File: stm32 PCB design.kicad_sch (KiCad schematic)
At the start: 13 parts, among them SW1 SW_SPDT, U1 STM32F103C8T6

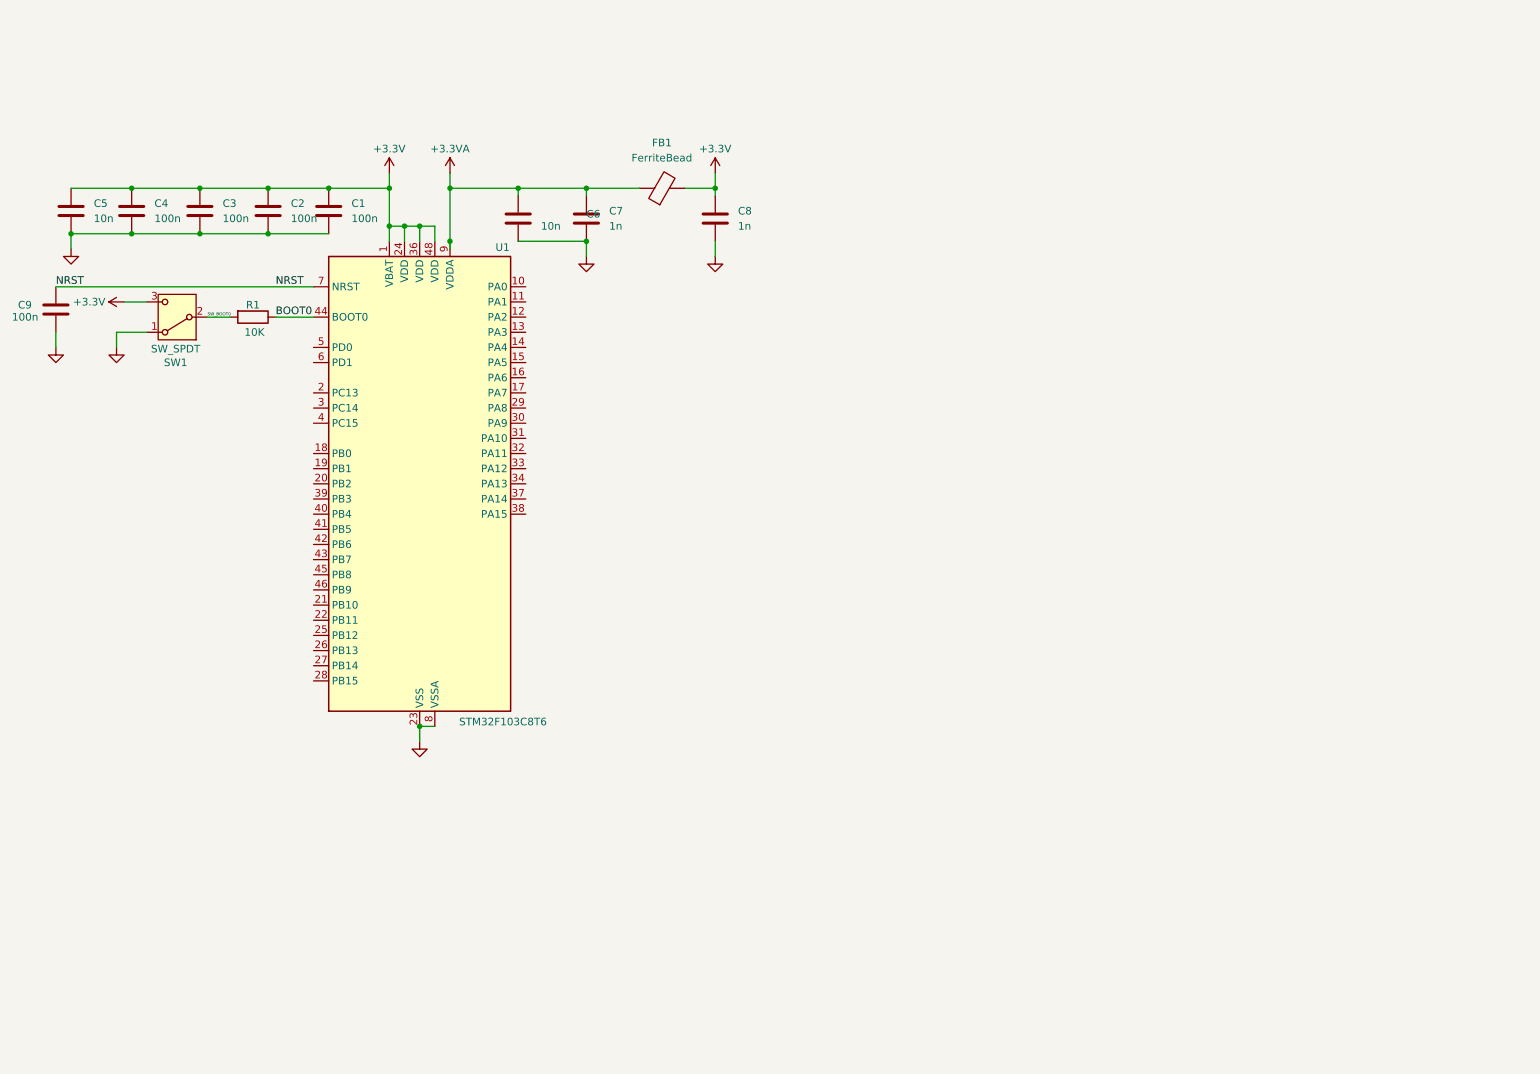
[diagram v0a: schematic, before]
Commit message: Schematic labelled and complete. EAD verified
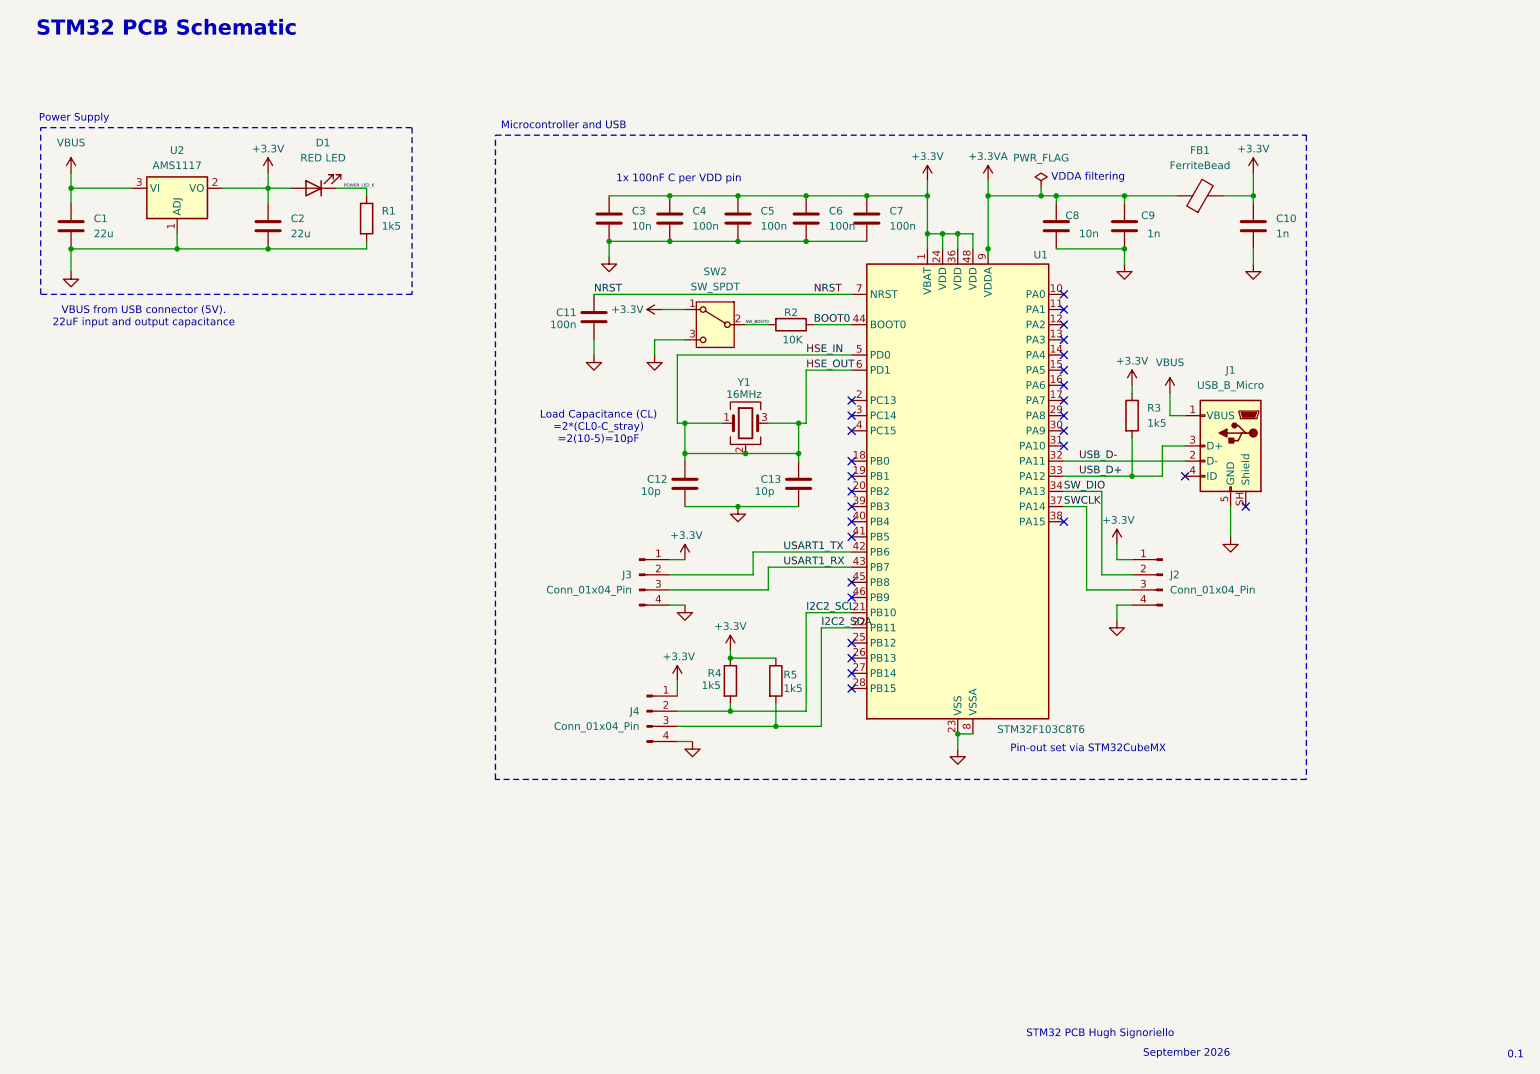
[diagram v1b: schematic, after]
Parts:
- removed SW1: SW_SPDT, symbol Switch:SW_SPDT
- added C1, C2: 22u, symbol Device:C
- added C12, C13: 10p, symbol Device:C
- added D1: RED LED, symbol Device:LED
- added J1: USB_B_Micro, symbol Connector:USB_B_Micro
- added J2, J3, J4: Conn_01x04_Pin, symbol Connector:Conn_01x04_Pin
- added R1, R3, R4, R5: 1k5, symbol Device:R
- added SW2: SW_SPDT, symbol Switch:SW_SPDT
- added U2: AMS1117, Package_TO_SOT_SMD:SOT-223-3_TabPin2, symbol Regulator_Linear:AMS1117
- added Y1: 16MHz, symbol Device:Crystal_GND24
- renumbered C8 to C10, C9 to C11, C5 to C3, C3 to C5, C2 to C6, C1 to C7, C6 to C8, C7 to C9, R1 to R2
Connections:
- net +3.3V: now also C2.1, D1.2 (A), J2.1 (Pin_1), J3.1 (Pin_1), J4.1 (Pin_1), R3.1, R4.1, R5.1, SW2.1 (A), U2.2 (VO)
- net SW_BOOT0: now also SW2.2 (B)
- net I2C2_SCL: now reaches U1.21 (PB10)
- net I2C2_SCL: now also J4.2 (Pin_2), R4.2
- net I2C2_SDA: now reaches U1.22 (PB11)
- net I2C2_SDA: now also J4.3 (Pin_3), R5.2
- net USB_D-: now reaches U1.32 (PA11)
- net USB_D-: now also J1.2 (D-)
- net USB_D+: now reaches U1.33 (PA12)
- net USB_D+: now also J1.3 (D+), R3.2
- net SW_DIO: now reaches U1.34 (PA13)
- net SW_DIO: now also J2.2 (Pin_2)
- net SWCLK: now reaches U1.37 (PA14)
- net SWCLK: now also J2.3 (Pin_3)
- net USART1_TX: now reaches U1.42 (PB6)
- net USART1_TX: now also J3.2 (Pin_2)
- net USART1_RX: now reaches U1.43 (PB7)
- net USART1_RX: now also J3.3 (Pin_3)
- net HSE_IN: now reaches U1.5 (PD0)
- net HSE_IN: now also U1.6 (PD1), C12.1, C13.1, Y1.1, Y1.2 (G), Y1.3, Y1.4 (G)
- new net: C1.2, C2.2, R1.2, U2.1 (ADJ)
- new net: C12.2, C13.2
- new net POWER_LED_K: D1.1 (K), R1.1
- new net VBUS: C1.1, J1.1 (VBUS), U2.3 (VI)
- no-connect marks 0 -> 29
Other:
- note added: "0.1"
- note added: "1x 100nF C per VDD pin"
- note added: "Load Capacitance (CL) =2*(CL0-C_stray) =2(10-5)=10pF"
- note added: "Microcontroller and USB"
- note added: "Pin-out set via STM32CubeMX"
- note added: "Power Supply"
- note added: "STM32 PCB Hugh Signoriello"
- note added: "STM32 PCB Schematic"
- note added: "September 2026"
- note added: "VBUS from USB connector (5V). 22uF input and output capacitance"
- note added: "VDDA filtering"
- moved on the sheet: C10, C11, C3, C4, C5, C6, C7, C8, C9, FB1, R2, U1

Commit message: Update PCB layout and add mounting holes
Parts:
- added H1, H2, H3, H4: MountingHole, MountingHole:MountingHole_2.2mm_M2, symbol Mechanical:MountingHole
- C1, C2: footprint (none) -> Capacitor_SMD:C_0805_2012Metric
- C10, C9: value 1n -> 1u; footprint (none) -> Capacitor_SMD:C_01005_0402Metric
- C11, C12, C13, C4, C5, C6, C7, C8: footprint (none) -> Capacitor_SMD:C_01005_0402Metric
- C3: footprint (none) -> Capacitor_SMD:C_0603_1608Metric
- D1: footprint (none) -> LED_SMD:LED_0603_1608Metric_Pad1.05x0.95mm_HandSolder
- FB1: footprint (none) -> Inductor_SMD:L_0603_1608Metric
- J1: footprint (none) -> Connector_USB:USB_Micro-B_Wuerth_629105150521
- J2, J3, J4: footprint (none) -> Connector_PinHeader_2.54mm:PinHeader_1x04_P2.54mm_Vertical
- R1, R2, R3, R4, R5: footprint (none) -> Resistor_SMD:R_0402_1005Metric
- SW2: footprint (none) -> Button_Switch_SMD:SW_SPDT_PCM12
- Y1: footprint (none) -> Crystal:Crystal_SMD_3225-4Pin_3.2x2.5mm
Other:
- note added: "Mounting Holes (M2)"

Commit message: Documentation updated and design rule checks validated
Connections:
- net HSE_IN: no longer C13.1, U1.6 (PD1), Y1.2 (G), Y1.3, Y1.4 (G)
- net GND: now reaches U1.23 (VSS), U1.35 (VSS), U1.47 (VSS), U1.8 (VSSA)
- net GND: now also C1.2, C10.2, C11.2, C12.2, C13.2, C2.2, C3.2, C4.2, C5.2, C6.2, C7.2, C8.2, C9.2, J1.5 (GND), J2.4 (Pin_4), J3.4 (Pin_4), J4.4 (Pin_4), R1.2, SW2.3 (C), U2.1 (ADJ), Y1.2 (G), Y1.4 (G)
- new net HSE_OUT: C13.1, U1.6 (PD1), Y1.3
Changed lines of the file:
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@@
 	)
 	(junction
-		(at 132.08 92.71)
-		(diameter 0)
-		(color 0 0 0 0)
-	)
-	(junction
 		(at 29.21 48.26)
 		(diameter 0)
@@
 	)
 	(junction
+		(at 142.24 101.6)
+		(diameter 0)
+		(color 0 0 0 0)
+	)
+	(junction
 		(at 46.99 58.42)
 		(diameter 0)
@@
 	)
 	(junction
-		(at 151.13 92.71)
-		(diameter 0)
-		(color 0 0 0 0)
-	)
-	(junction
-		(at 142.24 92.71)
-		(diameter 0)
-		(color 0 0 0 0)
-	)
-	(junction
 		(at 151.13 87.63)
 		(diameter 0)
@@
 	(wire
 		(pts
+			(xy 142.24 92.71) (xy 142.24 101.6)
+		)
+		(stroke
+			(width 0)
+			(type default)
+		)
+	)
+	(wire
+		(pts
 			(xy 199.39 115.57) (xy 207.01 115.57)
 		)
@@
 	(wire
 		(pts
-			(xy 142.24 92.71) (xy 151.13 92.71)
-		)
-		(stroke
-			(width 0)
-			(type default)
-		)
-	)
-	(wire
-		(pts
 			(xy 199.39 101.6) (xy 199.39 115.57)
 		)
@@
 	(wire
 		(pts
-			(xy 146.05 115.57) (xy 129.54 115.57)
+			(xy 142.24 101.6) (xy 151.13 101.6)
 		)
 		(stroke
@@
 	(wire
 		(pts
-			(xy 132.08 92.71) (xy 132.08 93.98)
+			(xy 146.05 115.57) (xy 129.54 115.57)
 		)
 		(stroke
@@
 	(wire
 		(pts
-			(xy 132.08 87.63) (xy 132.08 92.71)
+			(xy 132.08 87.63) (xy 132.08 93.98)
 		)
 		(stroke
@@
 	(wire
 		(pts
+			(xy 116.84 73.66) (xy 116.84 76.2)
+		)
+		(stroke
+			(width 0)
+			(type default)
+		)
+	)
+	(wire
+		(pts
 			(xy 147.32 138.43) (xy 154.94 138.43)
 		)
@@
 	(wire
 		(pts
-			(xy 151.13 87.63) (xy 151.13 92.71)
+			(xy 151.13 87.63) (xy 151.13 93.98)
 		)
 		(stroke
@@
 	(wire
 		(pts
-			(xy 116.84 73.66) (xy 116.84 76.2)
-		)
-		(stroke
-			(width 0)
-			(type default)
-		)
-	)
-	(wire
-		(pts
 			(xy 213.36 82.55) (xy 213.36 86.36)
 		)
@@
 	(wire
 		(pts
-			(xy 142.24 92.71) (xy 132.08 92.71)
-		)
-		(stroke
-			(width 0)
-			(type default)
-		)
-	)
-	(wire
-		(pts
 			(xy 128.27 68.58) (xy 132.08 68.58)
 		)
@@
 	(wire
 		(pts
-			(xy 151.13 92.71) (xy 151.13 93.98)
-		)
-		(stroke
-			(width 0)
-			(type default)
-		)
-	)
-	(wire
-		(pts
 			(xy 182.88 46.99) (xy 182.88 49.53)
 		)
@@
 	(wire
 		(pts
-			(xy 140.97 101.6) (xy 151.13 101.6)
+			(xy 140.97 101.6) (xy 142.24 101.6)
 		)
 		(stroke
@@
 			)
 		)
-		(property "Value" ""
+		(property "Value" "GND"
 			(at 127 81.28 0)
+			(hide yes)
 			(show_name no)
 			(do_not_autoplace no)
@@
 			)
 		)
-		(property "Value" ""
+		(property "Value" "GND"
 			(at 133.35 146.05 0)
+			(hide yes)
 			(show_name no)
 			(do_not_autoplace no)
@@
 			)
 		)
-		(property "Value" ""
+		(property "Value" "GND"
 			(at 223.52 111.76 0)
+			(hide yes)
 			(show_name no)
 			(do_not_autoplace no)
@@
 			)
 		)
-		(property "Value" ""
+		(property "Value" "GND"
 			(at 116.84 81.28 0)
+			(hide yes)
 			(show_name no)
 			(do_not_autoplace no)
@@
 			)
 		)
-		(property "Value" ""
+		(property "Value" "GND"
 			(at 29.21 67.31 0)
 			(show_name no)
@@
 			)
 		)
-		(property "Value" ""
+		(property "Value" "GND"
 			(at 204.47 125.73 0)
+			(hide yes)
 			(show_name no)
 			(do_not_autoplace no)
@@
 			)
 		)
-		(property "Value" ""
+		(property "Value" "GND"
 			(at 205.74 66.04 0)
+			(hide yes)
 			(show_name no)
 			(do_not_autoplace no)
@@
 			)
 		)
-		(property "Value" ""
+		(property "Value" "GND"
 			(at 119.38 64.77 0)
 			(show_name no)
@@
 			)
 		)
-		(property "Value" ""
+		(property "Value" "GND"
 			(at 177.8 147.32 0)
+			(hide yes)
 			(show_name no)
 			(do_not_autoplace no)
@@
 			)
 		)
-		(property "Value" ""
+		(property "Value" "GND"
 			(at 227.33 66.04 0)
+			(hide yes)
 			(show_name no)
 			(do_not_autoplace no)
@@
 			)
 		)
-		(property "Value" ""
+		(property "Value" "GND"
 			(at 132.08 123.19 0)
+			(hide yes)
 			(show_name no)
 			(do_not_autoplace no)
@@
 			)
 		)
-		(property "Value" ""
+		(property "Value" "GND"
 			(at 140.97 106.68 0)
+			(hide yes)
 			(show_name no)
 			(do_not_autoplace no)
